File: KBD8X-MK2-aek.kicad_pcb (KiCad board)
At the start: 2 copper layers, 343.7 x 118.3 mm, 214 parts, among them J1 AVR-ISP-6, Q1 DSS60601MZ4-13, SW1 SW_Push, U1 ATmega32U4-MU, U2 PRTR5V0U2X, Y1 16MHz

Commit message: finish routing bottom row
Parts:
- added D90: SOD-323, locallib:D_SOD-123, B.Cu at (231.8, 138.9)
- moved D81 21.8 mm to (275.0, 138.9)
- moved G*** 3.40 mm to (225.2, 138.1)
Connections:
- MX_RCTRL1 pad 1: (no net) -> Net-(D90-Pad2)
- MX_RCTRL1 pad 2: (no net) -> COL5
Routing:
- net COL3: track 448.7 -> 618.0 mm
- net COL2: track 321.6 -> 415.2 mm
- net COL4: track 343.9 -> 431.8 mm
- net COL5: track 310.8 -> 351.7 mm
- net COL1: track 295.0 -> 312.6 mm
- net Net-(D90-Pad2): track 0.00 -> 15.6 mm
- net Net-(D81-Pad2): track 20.1 -> 29.0 mm
- net Net-(RC2-Pad1): track 69.5 -> 74.6 mm
- net Net-(RC1-Pad2): track 67.5 -> 71.9 mm
- net ROW11: track 335.0 -> 337.9 mm
- net SLOCK_IND: track 51.5 -> 50.4 mm
- net COL8: track 165.1 -> 164.0 mm
- net D+: track 7.79 -> 7.05 mm
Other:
- outline, holes or cut-outs redrawn

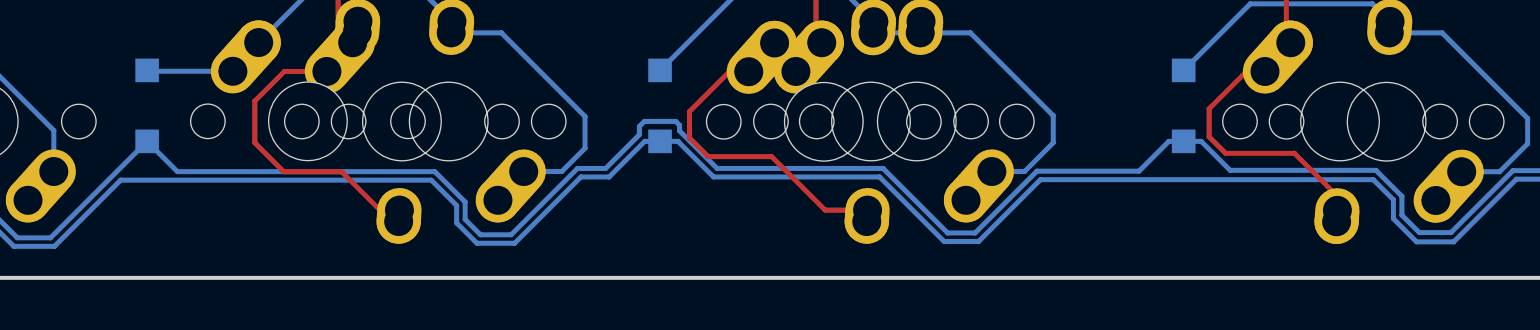
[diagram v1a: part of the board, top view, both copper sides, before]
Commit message: fix right bottom row to look even
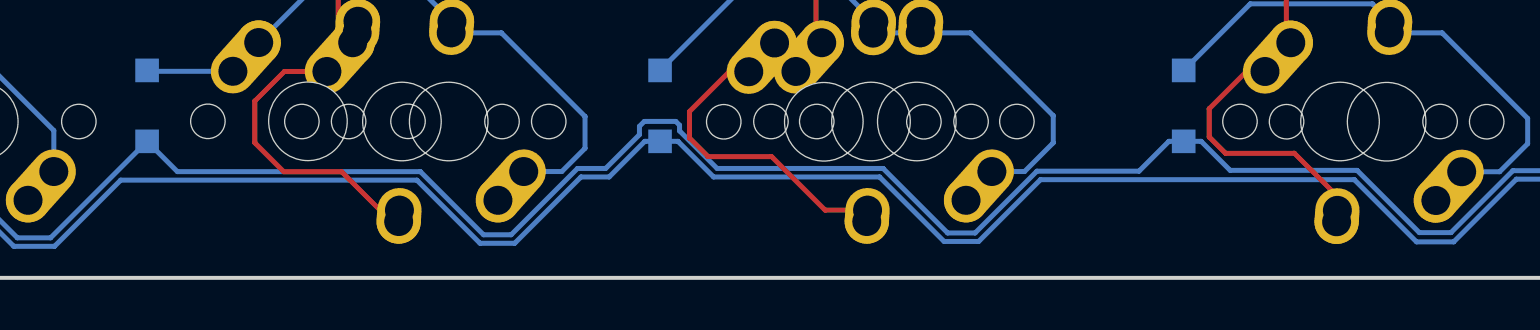
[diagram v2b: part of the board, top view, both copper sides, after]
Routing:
- net ROW10: track 354.2 -> 353.2 mm
- net ROW11: track 337.9 -> 336.8 mm
